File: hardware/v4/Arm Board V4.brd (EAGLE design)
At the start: 108 x 50.8 mm, 39 parts, among them IC3 L6206D, P1 STELLARIS-LAUNCHPADSTELLARIS-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, U1 SN74LS241DW, U2 XBEE-1B3

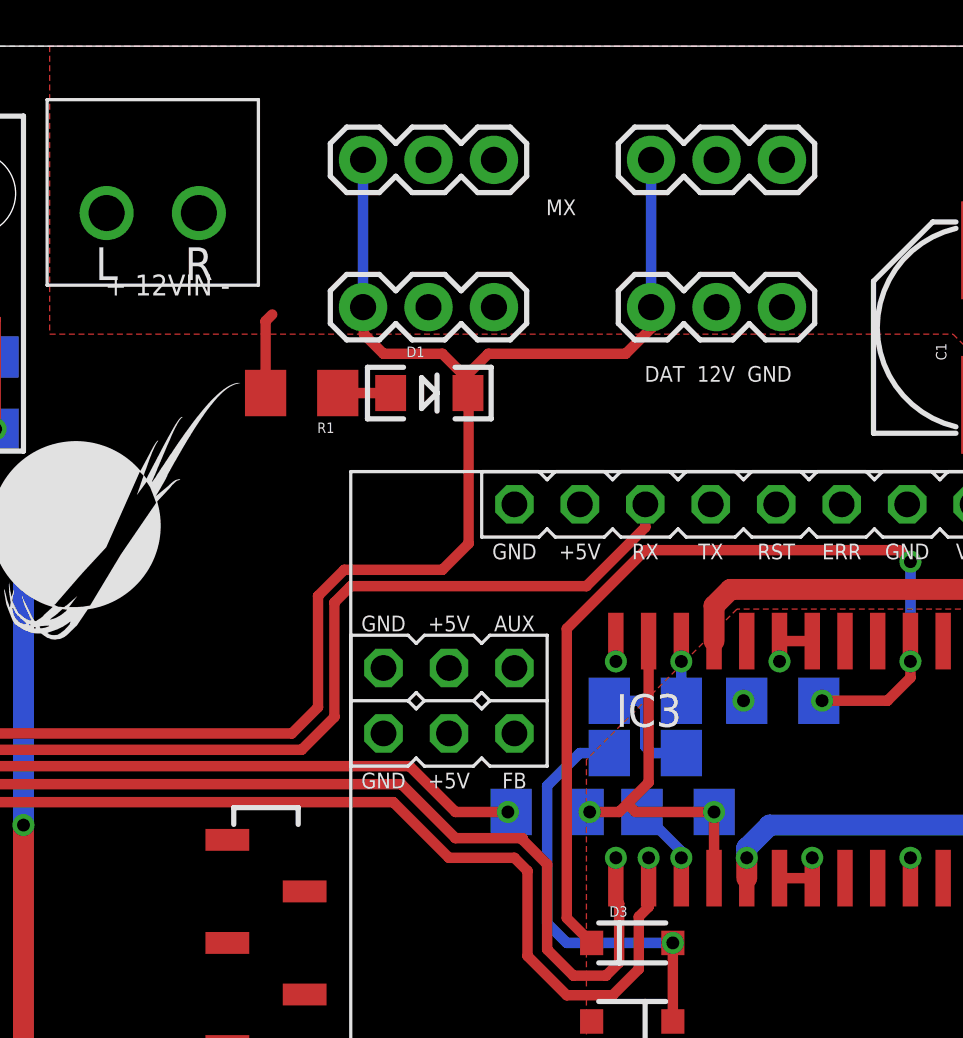
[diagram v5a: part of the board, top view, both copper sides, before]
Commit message: Added TVS diodes on Dyna data lines
Also added parts to BOM
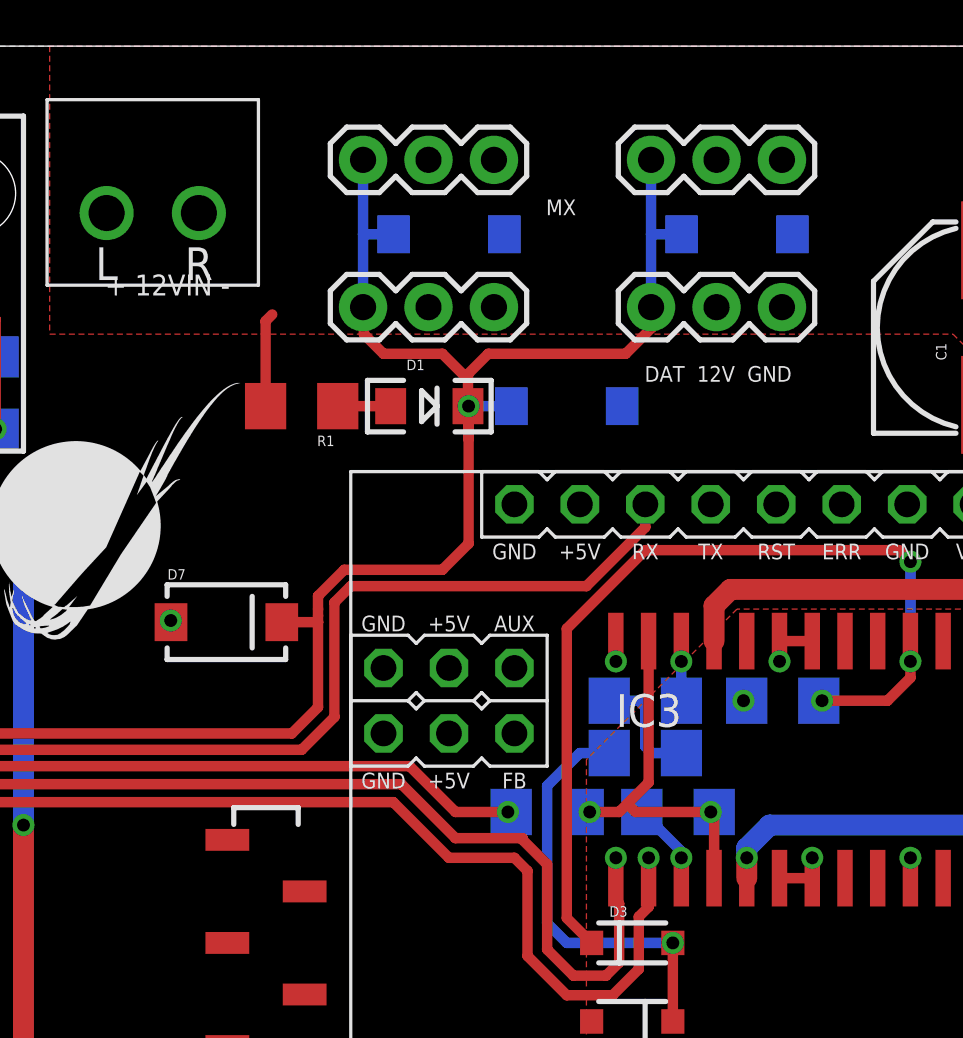
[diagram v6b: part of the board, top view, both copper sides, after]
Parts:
- added D4, D5, D6, D7: SMAJ5920, SparkFun-DiscreteSemi:SMA-DIODE
- moved D1 0.51 mm to (76.7, 36.8)
- moved R1 0.51 mm to (71.8, 36.8)
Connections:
- net DDATA_1: now also D4.C, D5.C, D6.C, D7.C
- net GND: now also D4.A, D5.A, D6.A, D7.A
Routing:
- net DDATA_1: track 113.8 -> 121.5 mm, vias 2 -> 3
- net +12V: track 3.28 -> 3.79 mm
- net GND: track 18.8 -> 18.9 mm, vias 12 -> 13
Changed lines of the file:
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@@
 <?xml version="1.0" encoding="utf-8"?>
 <!DOCTYPE eagle SYSTEM "eagle.dtd">
-<eagle version="6.5.0">
+<eagle version="7.0.0">
 <drawing>
 <settings>
@@
 <pass name="Default">
 <param name="RoutingGrid" value="50mil"/>
+<param name="AutoGrid" value="1"/>
+<param name="Efforts" value="0"/>
+<param name="TopRouterVariant" value="1"/>
 <param name="tpViaShape" value="round"/>
 <param name="PrefDir.1" value="|"/>
@@
 </element>
 <element name="U$1" library="MRDT-2015-Arm" package="TORXIS_BREAKOUT" value="TORXIS_BREAKOUT" x="107.95" y="0" rot="R90"/>
-<element name="R1" library="SparkFun-Resistors" package="1206" value="1k" x="71.755" y="37.338" rot="R180"/>
-<element name="D1" library="SparkFun-LED" package="LED-1206" value="RED" x="76.708" y="37.338"/>
+<element name="R1" library="SparkFun-Resistors" package="1206" value="1k" x="71.755" y="36.83" rot="R180"/>
+<element name="D1" library="SparkFun-LED" package="LED-1206" value="RED" x="76.708" y="36.83"/>
 <element name="IC3" library="L6206D" package="SO24" value="L6206D" x="90.932" y="23.114"/>
 <element name="R8" library="SparkFun-Resistors" package="1206" value="100k" x="81.28" y="21.082" rot="MR0"/>
@@
 </element>
 <element name="C1" library="SparkFun-Capacitors" package="PANASONIC_E" value="330uF" x="98.044" y="39.878" rot="R90"/>
+<element name="D4" library="SparkFun-DiscreteSemi" package="SMA-DIODE" value="SMAJ5920" x="77.47" y="43.4975" rot="MR0">
+<attribute name="PROD_ID" value="DIO-08053" x="77.47" y="43.4975" size="1.778" layer="28" rot="MR0" display="off"/>
+</element>
+<element name="D5" library="SparkFun-DiscreteSemi" package="SMA-DIODE" value="SMAJ5920" x="82.042" y="36.83" rot="MR0">
+<attribute name="PROD_ID" value="DIO-08053" x="82.042" y="36.83" size="1.778" layer="28" rot="MR0" display="off"/>
+</element>
+<element name="D6" library="SparkFun-DiscreteSemi" package="SMA-DIODE" value="SMAJ5920" x="88.646" y="43.4975" rot="MR0">
+<attribute name="PROD_ID" value="DIO-08053" x="88.646" y="43.4975" size="1.778" layer="28" rot="MR0" display="off"/>
+</element>
+<element name="D7" library="SparkFun-DiscreteSemi" package="SMA-DIODE" value="SMAJ5920" x="68.834" y="28.448">
+<attribute name="PROD_ID" value="DIO-08053" x="68.834" y="28.448" size="1.778" layer="27" display="off"/>
+</element>
 </elements>
 <signals>
@@
 <wire x1="48.895" y1="36.195" x2="48.895" y2="37.465" width="0.8128" layer="1"/>
 <wire x1="48.895" y1="37.465" x2="50.165" y2="38.735" width="0.8128" layer="1"/>
+<contactref element="D7" pad="A"/>
+<contactref element="D6" pad="A"/>
+<contactref element="D5" pad="A"/>
+<contactref element="D4" pad="A"/>
+<via x="66.675" y="28.5115" extent="1-16" drill="0.5"/>
+<wire x1="66.684" y1="28.448" x2="66.675" y2="28.448" width="0.4064" layer="1"/>
+<wire x1="66.675" y1="28.448" x2="66.675" y2="28.5115" width="0.4064" layer="1"/>
 </signal>
 <signal name="+3V3">
@@
 <contactref element="C1" pad="+"/>
 <contactref element="R1" pad="2"/>
-<wire x1="70.355" y1="37.338" x2="70.355" y2="40.129" width="0.4064" layer="1"/>
+<wire x1="70.355" y1="36.83" x2="70.355" y2="40.129" width="0.4064" layer="1"/>
 <wire x1="70.355" y1="40.129" x2="70.612" y2="40.386" width="0.4064" layer="1"/>
 </signal>
@@
 <contactref element="D1" pad="C"/>
 <wire x1="16.38935" y1="14.85265" x2="15.24" y2="14.85265" width="0.4064" layer="1"/>
-<wire x1="78.208" y1="37.338" x2="78.208" y2="37.87" width="0.4064" layer="1"/>
+<wire x1="78.208" y1="36.83" x2="78.208" y2="37.87" width="0.4064" layer="1"/>
 <wire x1="78.208" y1="37.87" x2="77.216" y2="38.862" width="0.4064" layer="1"/>
 <wire x1="77.216" y1="38.862" x2="74.93" y2="38.862" width="0.4064" layer="1"/>
@@
 <wire x1="85.344" y1="39.878" x2="85.344" y2="40.64" width="0.4064" layer="1"/>
 <wire x1="85.344" y1="40.64" x2="85.31225" y2="40.67175" width="0.4064" layer="1"/>
-<wire x1="72.39" y1="25.146" x2="72.39" y2="29.464" width="0.4064" layer="1"/>
+<wire x1="72.39" y1="25.146" x2="72.39" y2="28.448" width="0.4064" layer="1"/>
+<wire x1="72.39" y1="28.956" x2="72.39" y2="29.464" width="0.4064" layer="1"/>
 <wire x1="72.39" y1="29.464" x2="73.406" y2="30.48" width="0.4064" layer="1"/>
 <wire x1="73.406" y1="30.48" x2="77.216" y2="30.48" width="0.4064" layer="1"/>
 <wire x1="77.216" y1="30.48" x2="78.232" y2="31.496" width="0.4064" layer="1"/>
-<wire x1="78.232" y1="31.496" x2="78.232" y2="37.314" width="0.4064" layer="1"/>
-<wire x1="78.232" y1="37.314" x2="78.208" y2="37.338" width="0.4064" layer="1"/>
-<wire x1="74.13625" y1="40.67175" x2="74.13625" y2="46.38675" width="0.4064" layer="16"/>
-<wire x1="85.31225" y1="40.67175" x2="85.31225" y2="46.38675" width="0.4064" layer="16"/>
+<wire x1="78.232" y1="31.496" x2="78.232" y2="36.83" width="0.4064" layer="1"/>
+<wire x1="78.232" y1="36.83" x2="78.232" y2="37.314" width="0.4064" layer="1"/>
+<wire x1="78.232" y1="37.314" x2="78.208" y2="36.83" width="0.4064" layer="1"/>
+<wire x1="74.13625" y1="40.67175" x2="74.13625" y2="43.4975" width="0.4064" layer="16"/>
+<wire x1="74.13625" y1="43.4975" x2="74.13625" y2="46.38675" width="0.4064" layer="16"/>
+<wire x1="85.31225" y1="40.67175" x2="85.31225" y2="43.4975" width="0.4064" layer="16"/>
+<contactref element="D5" pad="C"/>
+<contactref element="D6" pad="C"/>
+<contactref element="D7" pad="C"/>
+<contactref element="D4" pad="C"/>
+<wire x1="85.31225" y1="43.4975" x2="85.31225" y2="46.38675" width="0.4064" layer="16"/>
+<wire x1="70.984" y1="28.448" x2="72.39" y2="28.448" width="0.4064" layer="1"/>
+<wire x1="72.39" y1="28.448" x2="72.39" y2="28.702" width="0.4064" layer="1"/>
+<wire x1="75.32" y1="43.4975" x2="74.13625" y2="43.4975" width="0.4064" layer="16"/>
+<wire x1="86.496" y1="43.4975" x2="85.31225" y2="43.4975" width="0.4064" layer="16"/>
+<wire x1="79.892" y1="36.83" x2="78.232" y2="36.83" width="0.4064" layer="16"/>
+<via x="78.232" y="36.83" extent="1-16" drill="0.5"/>
+<wire x1="78.232" y1="36.83" x2="78.232" y2="35.56" width="0.4064" layer="1"/>
+<wire x1="72.39" y1="28.702" x2="72.39" y2="28.956" width="0.4064" layer="1"/>
 </signal>
 <signal name="N$7">
@@
 <contactref element="R1" pad="1"/>
 <contactref element="D1" pad="A"/>
-<wire x1="75.208" y1="37.338" x2="73.155" y2="37.338" width="0.4064" layer="1"/>
+<wire x1="75.208" y1="36.83" x2="73.155" y2="36.83" width="0.4064" layer="1"/>
 </signal>
 <signal name="A1">
@@
 <wire x1="85.217" y1="22.225" x2="85.217" y2="27.714" width="0.4064" layer="1"/>
 <wire x1="84.709" y1="21.082" x2="84.3915" y2="21.3995" width="0.4064" layer="1"/>
-<wire x1="87.757" y1="18.514" x2="87.757" y2="21.079" width="0.4064" layer="1"/>
-<wire x1="87.757" y1="21.079" x2="87.76" y2="21.082" width="0.4064" layer="1"/>
-<wire x1="87.76" y1="21.082" x2="87.757" y2="21.082" width="0.4064" layer="1"/>
-<wire x1="87.757" y1="21.082" x2="84.709" y2="21.082" width="0.4064" layer="1"/>
-<via x="87.757" y="21.082" extent="1-16" drill="0.5"/>
 <via x="82.931" y="21.082" extent="1-16" drill="0.5"/>
 <wire x1="82.931" y1="21.082" x2="84.074" y2="21.082" width="0.4064" layer="1"/>
+<wire x1="87.757" y1="18.514" x2="87.76" y2="18.514" width="0.4064" layer="1"/>
+<wire x1="87.76" y1="18.514" x2="87.76" y2="21.082" width="0.4064" layer="1"/>
+<wire x1="87.76" y1="21.082" x2="87.63" y2="21.082" width="0.4064" layer="1"/>
+<via x="87.63" y="21.082" extent="1-16" drill="0.5"/>
+<wire x1="84.709" y1="21.082" x2="87.63" y2="21.082" width="0.4064" layer="1"/>
 <wire x1="87.76" y1="21.082" x2="87.76" y2="21.082" width="0" layer="19" extent="1-16"/>
 </signal>

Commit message: added some trace names
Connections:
- net N$1 renamed TX-
- net N$2 renamed RX-
- net N$3 renamed RX+
- net N$5 renamed TX+
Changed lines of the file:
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@@
 <?xml version="1.0" encoding="utf-8"?>
 <!DOCTYPE eagle SYSTEM "eagle.dtd">
-<eagle version="7.0.0">
+<eagle version="6.5.0">
 <drawing>
 <settings>
@@
 <layer number="223" name="223bmp" color="24" fill="1" visible="no" active="no"/>
 <layer number="224" name="224bmp" color="25" fill="1" visible="no" active="no"/>
-<layer number="225" name="225bmp" color="7" fill="1" visible="yes" active="yes"/>
-<layer number="226" name="226bmp" color="7" fill="1" visible="yes" active="yes"/>
-<layer number="227" name="227bmp" color="7" fill="1" visible="yes" active="yes"/>
-<layer number="228" name="228bmp" color="7" fill="1" visible="yes" active="yes"/>
-<layer number="229" name="229bmp" color="7" fill="1" visible="yes" active="yes"/>
-<layer number="230" name="230bmp" color="7" fill="1" visible="yes" active="yes"/>
+<layer number="225" name="225bmp" color="7" fill="1" visible="no" active="yes"/>
+<layer number="226" name="226bmp" color="7" fill="1" visible="no" active="yes"/>
+<layer number="227" name="227bmp" color="7" fill="1" visible="no" active="yes"/>
+<layer number="228" name="228bmp" color="7" fill="1" visible="no" active="yes"/>
+<layer number="229" name="229bmp" color="7" fill="1" visible="no" active="yes"/>
+<layer number="230" name="230bmp" color="7" fill="1" visible="no" active="yes"/>
 <layer number="231" name="Eagle3D_PG1" color="7" fill="1" visible="no" active="no"/>
 <layer number="232" name="Eagle3D_PG2" color="7" fill="1" visible="no" active="no"/>
@@
 <layer number="251" name="SMDround" color="12" fill="11" visible="no" active="no"/>
 <layer number="254" name="cooling" color="7" fill="1" visible="no" active="no"/>
-<layer number="255" name="routoute" color="7" fill="1" visible="yes" active="yes"/>
+<layer number="255" name="routoute" color="7" fill="1" visible="no" active="yes"/>
 </layers>
 <board>
@@
 <pass name="Default">
 <param name="RoutingGrid" value="50mil"/>
-<param name="AutoGrid" value="1"/>
-<param name="Efforts" value="0"/>
-<param name="TopRouterVariant" value="1"/>
 <param name="tpViaShape" value="round"/>
 <param name="PrefDir.1" value="|"/>
@@
 <wire x1="45.466" y1="22.9205" x2="45.7835" y2="23.238" width="0.4064" layer="1"/>
 </signal>
-<signal name="N$5">
+<signal name="TX+">
 <contactref element="U$3" pad="1"/>
 <contactref element="R11" pad="2"/>
@@
 <wire x1="58.166" y1="38.354" x2="57.785" y2="38.735" width="0.4064" layer="1"/>
 </signal>
-<signal name="N$1">
+<signal name="TX-">
 <contactref element="U$3" pad="2"/>
 <contactref element="R11" pad="1"/>
@@
 <wire x1="56.772" y1="35.938" x2="56.515" y2="36.195" width="0.4064" layer="16"/>
 </signal>
-<signal name="N$2">
+<signal name="RX-">
 <contactref element="U$3" pad="6"/>
 <contactref element="R10" pad="2"/>
@@
 <wire x1="50.927" y1="36.195" x2="51.435" y2="36.195" width="0.4064" layer="16"/>
 </signal>
-<signal name="N$3">
+<signal name="RX+">
 <contactref element="U$3" pad="3"/>
 <contactref element="R10" pad="1"/>

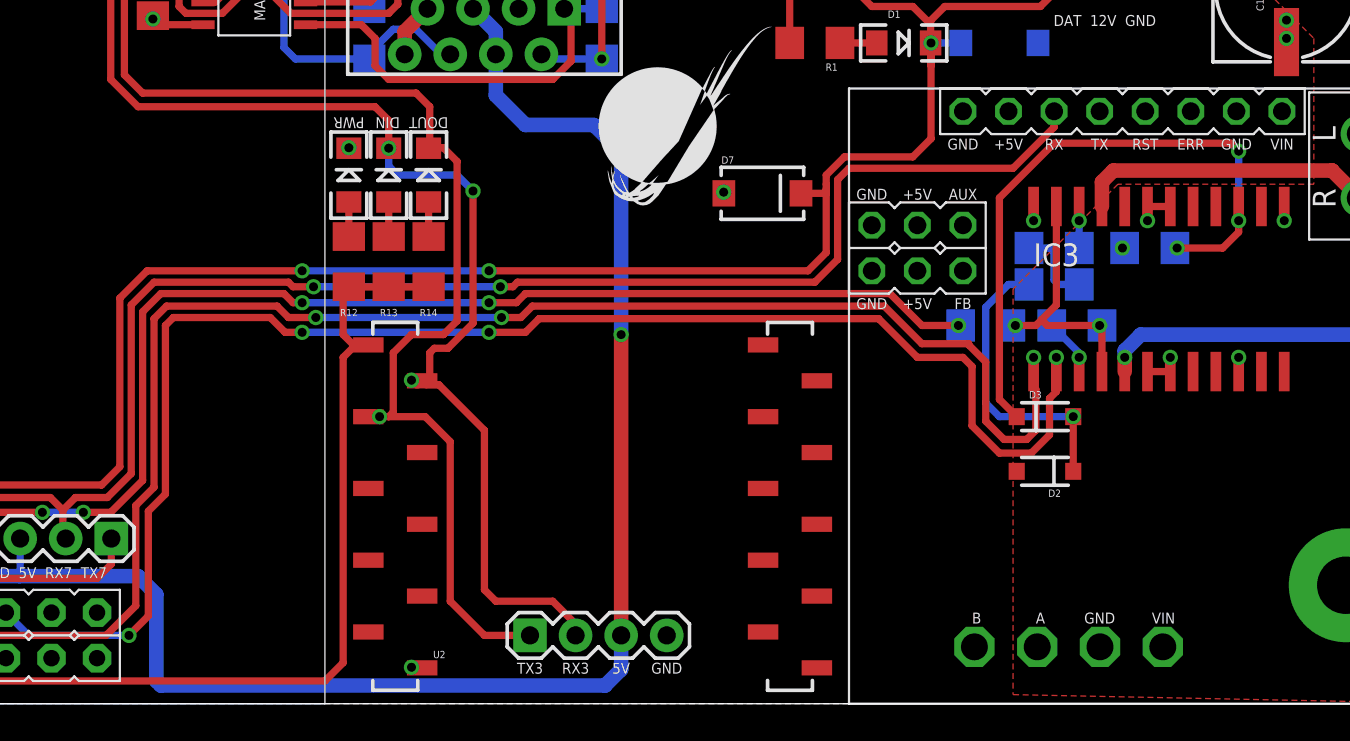
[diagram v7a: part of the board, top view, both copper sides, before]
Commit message: fixed RX/TX issue between Tiva C and Pololu Jrk 21v3
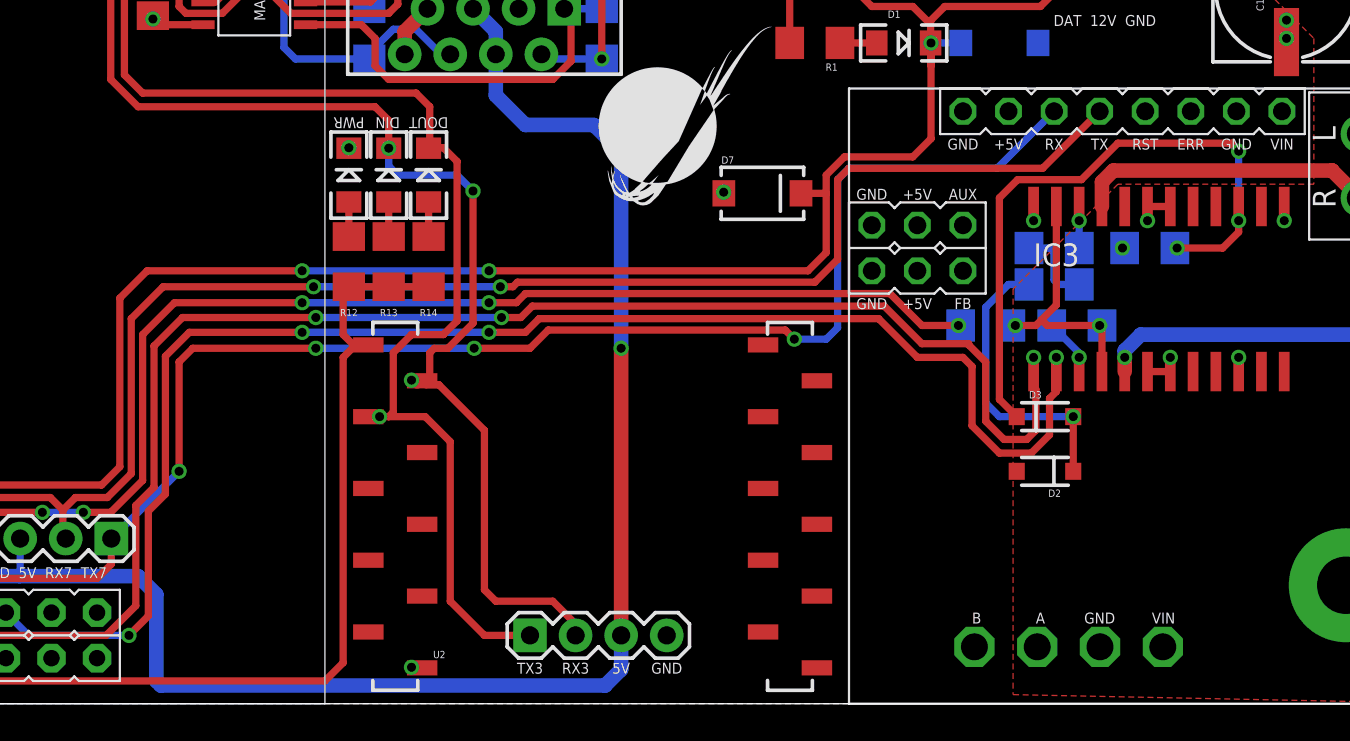
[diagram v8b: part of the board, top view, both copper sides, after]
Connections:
- net RX_7: now also U$1.TX; no longer U$1.RX
- net TX_7: now also U$1.RX
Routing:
- net TX_7: track 11.3 -> 82.6 mm, vias 0 -> 4
- net IN2_A: track 85.6 -> 83.9 mm
- net IN1_A: track 89.5 -> 88.1 mm
- net RX_7: track 134.7 -> 136.0 mm
- net EN_A: track 89.7 -> 88.5 mm
